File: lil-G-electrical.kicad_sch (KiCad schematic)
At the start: 39 parts, among them J1 GPIO, J2 XT-60, Q1 STD26P3LLH6, SW1 B3J-1000, SW2 PVA1EE, U1 TPS565208, U2 CAT24C256, U3 LTC2955-1, U4 MCP1415

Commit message: small update on schematic
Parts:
- renumbered C13 to C1, C3 to C10, C5 to C11, C6 to C12, C7 to C13, C11 to C2, C8 to C3, C10 to C4, C12 to C5, C9 to C6, C4 to C7, C1 to C8, C2 to C9, J2 to J1, J1 to J2, R6 to R1, R2 to R10, R3 to R11, R4 to R12, R8 to R2, R10 to R3, R12 to R4, R7 to R5, R9 to R6, R11 to R7, R5 to R8, R1 to R9, U3 to U1, U4 to U2, U1 to U3, U2 to U4
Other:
- moved on the sheet: C13, JP1, R11, R12, U4

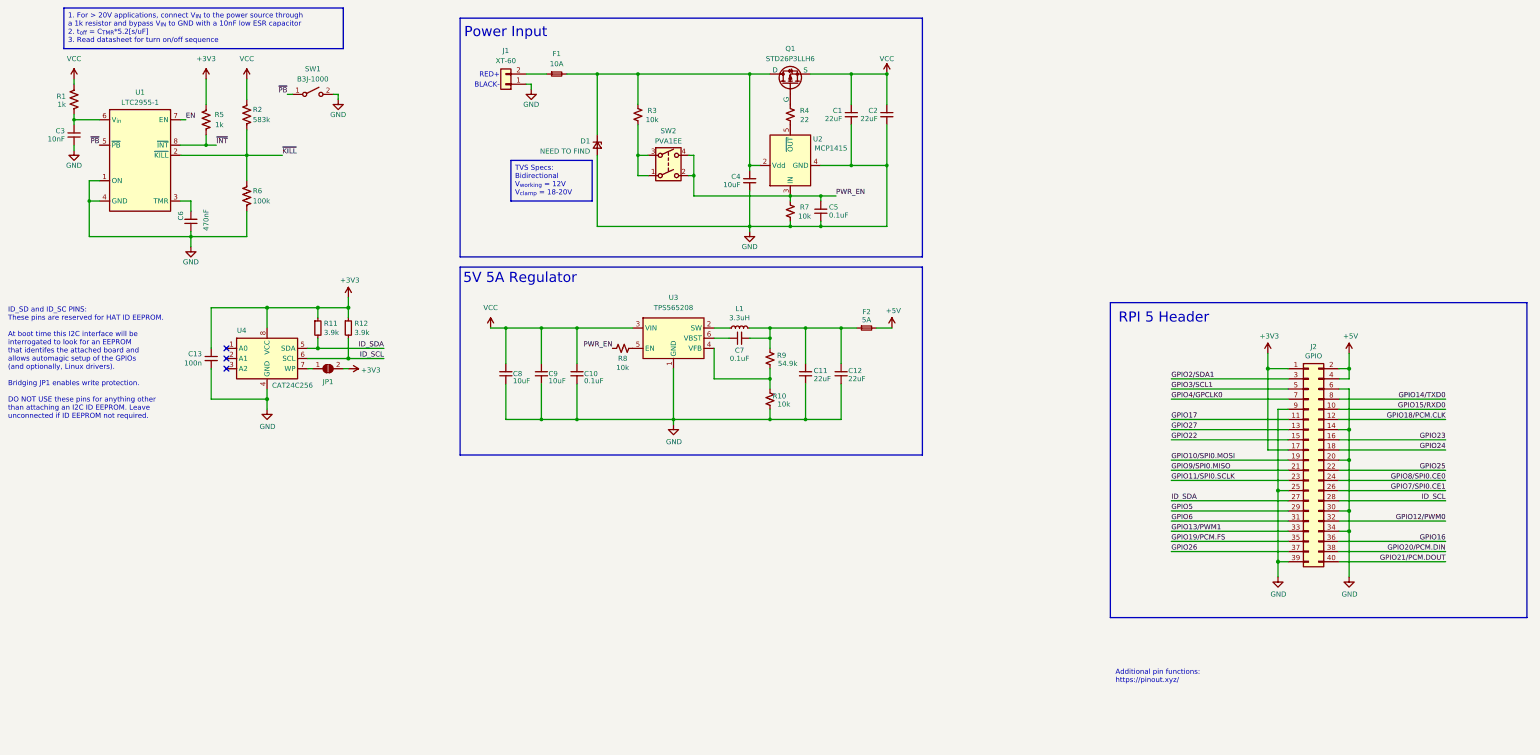
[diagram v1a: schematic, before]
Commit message: finished layout of dc drivers and power regulation
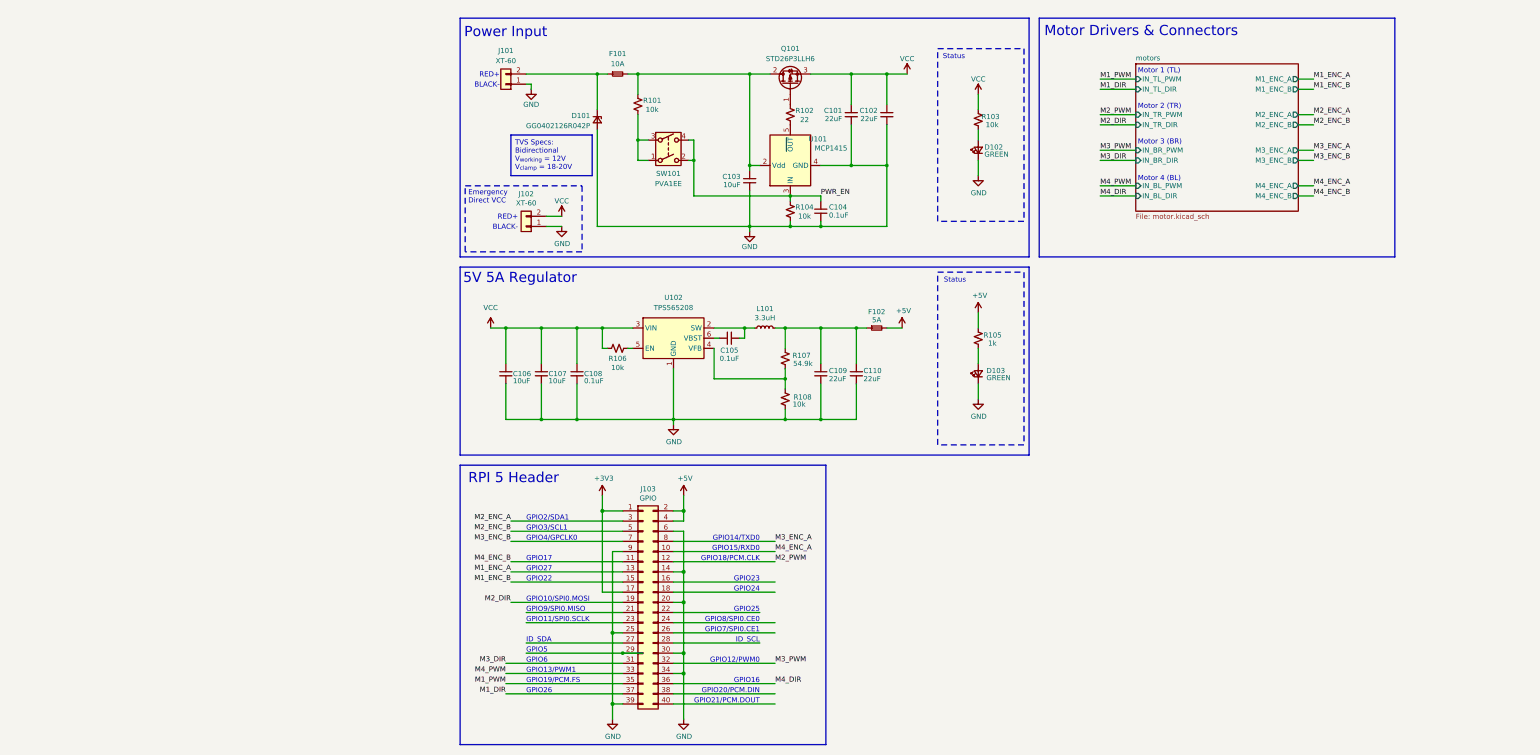
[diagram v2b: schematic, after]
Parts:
- removed C13: 100n, symbol Device:C_Small
- removed C3: 10nF, Capacitor_SMD:C_0603_1608Metric, symbol Device:C_Small
- removed C6: 470nF, Capacitor_SMD:C_1206_3216Metric, symbol Device:C_Small
- removed JP1: ID_WP, symbol Jumper:SolderJumper_2_Open
- removed Q1: STD26P3LLH6, Package_TO_SOT_SMD:TO-252-2, symbol Simulation_SPICE:PMOS
- removed R1, R5: 1k, Resistor_SMD:R_0603_1608Metric, symbol Device:R_US
- removed R11, R12: 3.9k, symbol Device:R_Small
- removed R2: 583k, Resistor_SMD:R_0603_1608Metric, symbol Device:R_US
- removed R6: 100k, Resistor_SMD:R_0603_1608Metric, symbol Device:R_US
- removed SW1: B3J-1000, RoboJackets-Switches:B3J-1000, symbol Switch:SW_SPST
- removed U1: LTC2955-1, RoboJackets-Power:SOT65P280X100-8N, symbol RoboJackets-Power:LTC2955-1
- removed U4: CAT24C256, symbol Memory_EEPROM:CAT24C256
- added D102, D103: GREEN, LED_SMD:LED_0603_1608Metric, symbol Device:LED_Small
- added J102: XT-60, Connector_AMASS:AMASS_XT60-M_1x02_P7.20mm_Vertical, symbol Connector_Generic:Conn_01x02
- added Q101: STD26P3LLH6, Package_TO_SOT_SMD:TO-252-2, symbol Device:Q_PMOS_GDS
- added R103: 10k, Resistor_SMD:R_0603_1608Metric, symbol Device:R_Small_US
- added R105: 1k, Resistor_SMD:R_0603_1608Metric, symbol Device:R_Small_US
- D101: renamed from D1; value NEED TO FIND -> GG0402126R042P; footprint Diode_SMD:D_0603_1608Metric -> Diode_SMD:D_0402_1005Metric
- F102: renamed from F2; footprint lilG_footprints:LittleFuse_Mini_100_SMD -> Fuse:Fuse_0603_1608Metric; MPN (none) -> F0603SB5000V032TM
- R101: renamed from R3; footprint (none) -> Resistor_SMD:R_0603_1608Metric
- R102: renamed from R4; footprint (none) -> Resistor_SMD:R_0603_1608Metric
- R104: renamed from R7; footprint (none) -> Resistor_SMD:R_0603_1608Metric
- R106: renamed from R8; footprint (none) -> Resistor_SMD:R_0603_1608Metric
- R107: renamed from R9; footprint (none) -> Resistor_SMD:R_0603_1608Metric
- R108: renamed from R10; footprint (none) -> Resistor_SMD:R_0603_1608Metric
- U102: renamed from U3; footprint Package_SO:Texas_R-PDSO-G8_EP2.95x4.9mm_Mask2.4x3.1mm -> Package_TO_SOT_SMD:SOT-23-6
- renumbered C1 to C101, C2 to C102, C4 to C103, C5 to C104, C7 to C105, C8 to C106, C9 to C107, C10 to C108, C11 to C109, C12 to C110, F1 to F101, J1 to J101, J2 to J103, L1 to L101, SW2 to SW101, U2 to U101
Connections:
- net +5V: now also R105.2
- net GND: now also D102.1 (K), D103.1 (K), J102.1 (Pin_1)
- net PWR_EN: no longer R106.2
- net VCC: now also R106.2, J102.2 (Pin_2), Q101.3 (S), R103.2
- net at C103.1, F101.2, R101.1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: now also Q101.2 (D); no longer D101.1 (K)
- net at F101.1, J101.2 (Pin_2): now also D101.1 (K)
- net at C109.1, C110.1, F102.1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: no longer C105.1
- net at L101.1, U102.2 (SW): now also C105.1
- net at R102.1: now also Q101.1 (G)
- net GPIO10/SPI0.MOSI renamed M2_DIR
- net GPIO11/SPI0.SCLK: no longer names the net of J103.23 (Pin_23)
- net GPIO12/PWM0 renamed M3_PWM
- net GPIO13/PWM1 renamed M4_PWM
- net GPIO14/TXD0 renamed M3_ENC_A
- net GPIO15/RXD0 renamed M4_ENC_A
- net GPIO16 renamed M4_DIR
- net GPIO17 renamed M4_ENC_B
- net GPIO18/PCM.CLK renamed M2_PWM
- net GPIO19/PCM.FS renamed M1_PWM
- net GPIO20/PCM.DIN: no longer names the net of J103.38 (Pin_38)
- net GPIO21/PCM.DOUT: no longer names the net of J103.40 (Pin_40)
- net GPIO22 renamed M1_ENC_B
- net GPIO23: no longer names the net of J103.16 (Pin_16)
- net GPIO24: no longer names the net of J103.18 (Pin_18)
- net GPIO25: no longer names the net of J103.22 (Pin_22)
- net GPIO26 renamed M1_DIR
- net GPIO27 renamed M1_ENC_A
- net GPIO2/SDA1 renamed M2_ENC_A
- net GPIO3/SCL1 renamed M2_ENC_B
- net GPIO4/GPCLK0 renamed M3_ENC_B
- net GPIO5: no longer names the net of J103.29 (Pin_29)
- net GPIO6 renamed M3_DIR
- net GPIO7/SPI0.CE1: no longer names the net of J103.26 (Pin_26)
- net GPIO8/SPI0.CE0: no longer names the net of J103.24 (Pin_24)
- net GPIO9/SPI0.MISO: no longer names the net of J103.21 (Pin_21)
- net ID_SCL: no longer names the net of J103.28 (Pin_28)
- net ID_SDA: no longer names the net of J103.27 (Pin_27)
- new net: D102.2 (A), R103.1
- new net: D103.2 (A), R105.1
- no-connect marks 3 -> 0
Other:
- added sheet motors (motor.kicad_sch)
- note added: "Emergency Direct VCC"
- note added: "GPIO10/SPI0.MOSI"
- note added: "GPIO11/SPI0.SCLK"
- note added: "GPIO12/PWM0"
- note added: "GPIO13/PWM1"
- note added: "GPIO14/TXD0"
- note added: "GPIO15/RXD0"
- note added: "GPIO16"
- note added: "GPIO17"
- note added: "GPIO18/PCM.CLK"
- note added: "GPIO19/PCM.FS"
- note added: "GPIO2/SDA1"
- note added: "GPIO20/PCM.DIN"
- note added: "GPIO21/PCM.DOUT"
- note added: "GPIO22"
- note added: "GPIO23"
- note added: "GPIO24"
- note added: "GPIO25"
- note added: "GPIO26"
- note added: "GPIO27"
- note added: "GPIO3/SCL1"
- note added: "GPIO4/GPCLK0"
- note added: "GPIO5"
- note added: "GPIO6"
- note added: "GPIO7/SPI0.CE1"
- note added: "GPIO8/SPI0.CE0"
- note added: "GPIO9/SPI0.MISO"
- note added: "ID_SCL"
- note added: "ID_SDA"
- note added: "Motor 1 (TL)"
- note added: "Motor 2 (TR)"
- note added: "Motor 3 (BR)"
- note added: "Motor 4 (BL)"
- note added: "Motor Drivers & Connectors"
- note added: "Status"
- note removed: "Additional pin functions: https://pinout.xyz/"
- note removed: "ID_SD and ID_SC PINS: These pins are reserved for HAT ID EEPROM. At boot time this I2C interface will be interrogated to look for an EEPROM that identifes the attached board and allows automagic setup of the GPIOs (and optionally, Linux drivers). Bridging JP1 enables write protection. DO NOT USE these pins for anything other than attaching an I2C ID EEPROM. Leave unconnected if ID EEPROM not requ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"
- moved on the sheet: C105, C109, C110, D101, F101, F102, J103, L101, R101, R106, R107, R108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

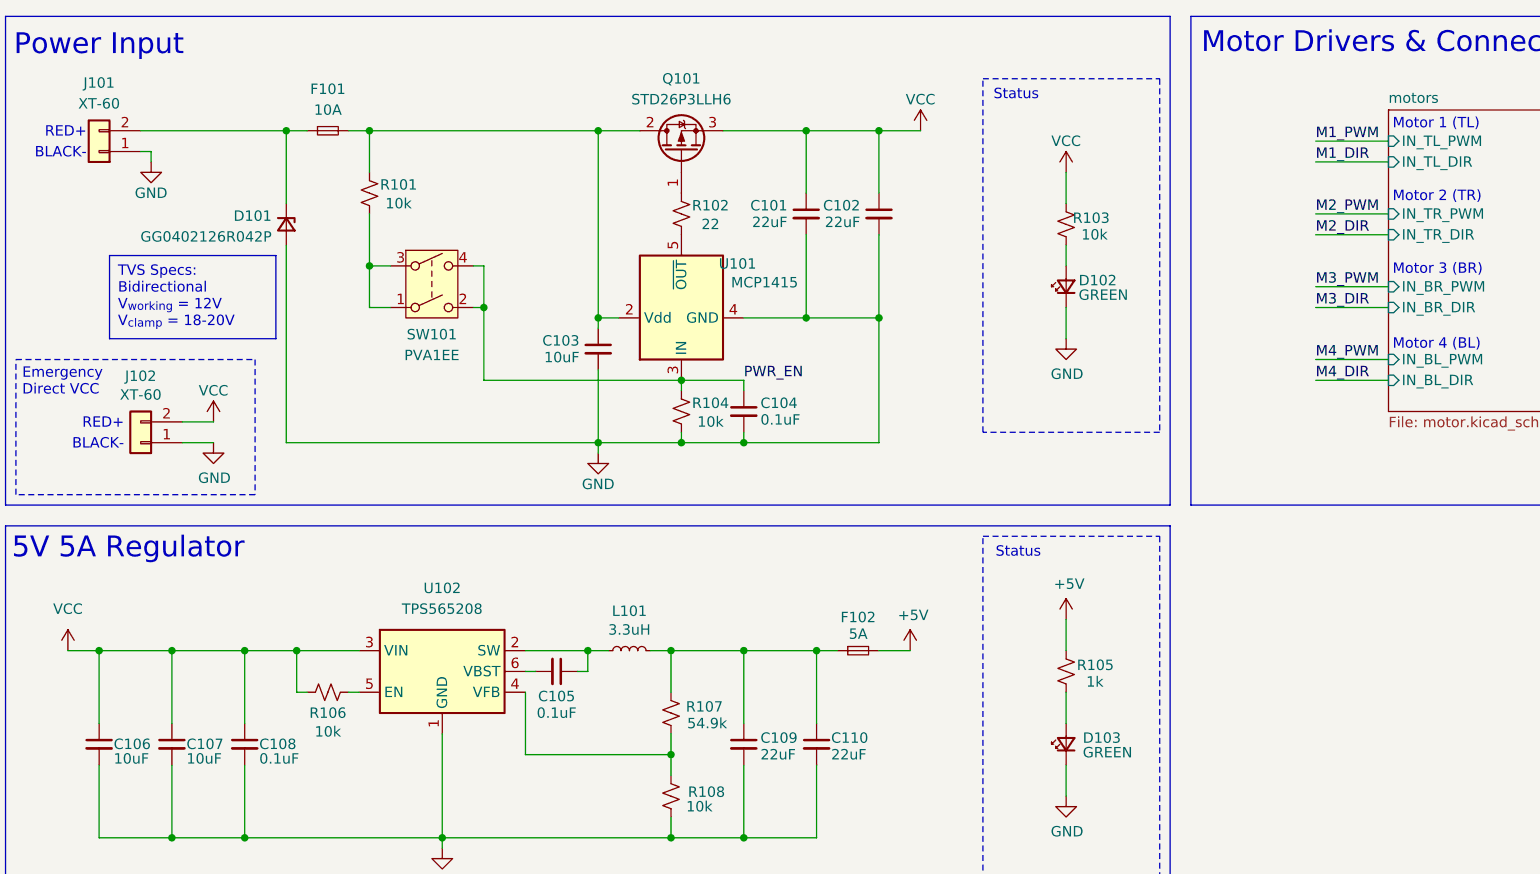
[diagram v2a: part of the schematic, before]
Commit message: changed dimension of current sense resistor
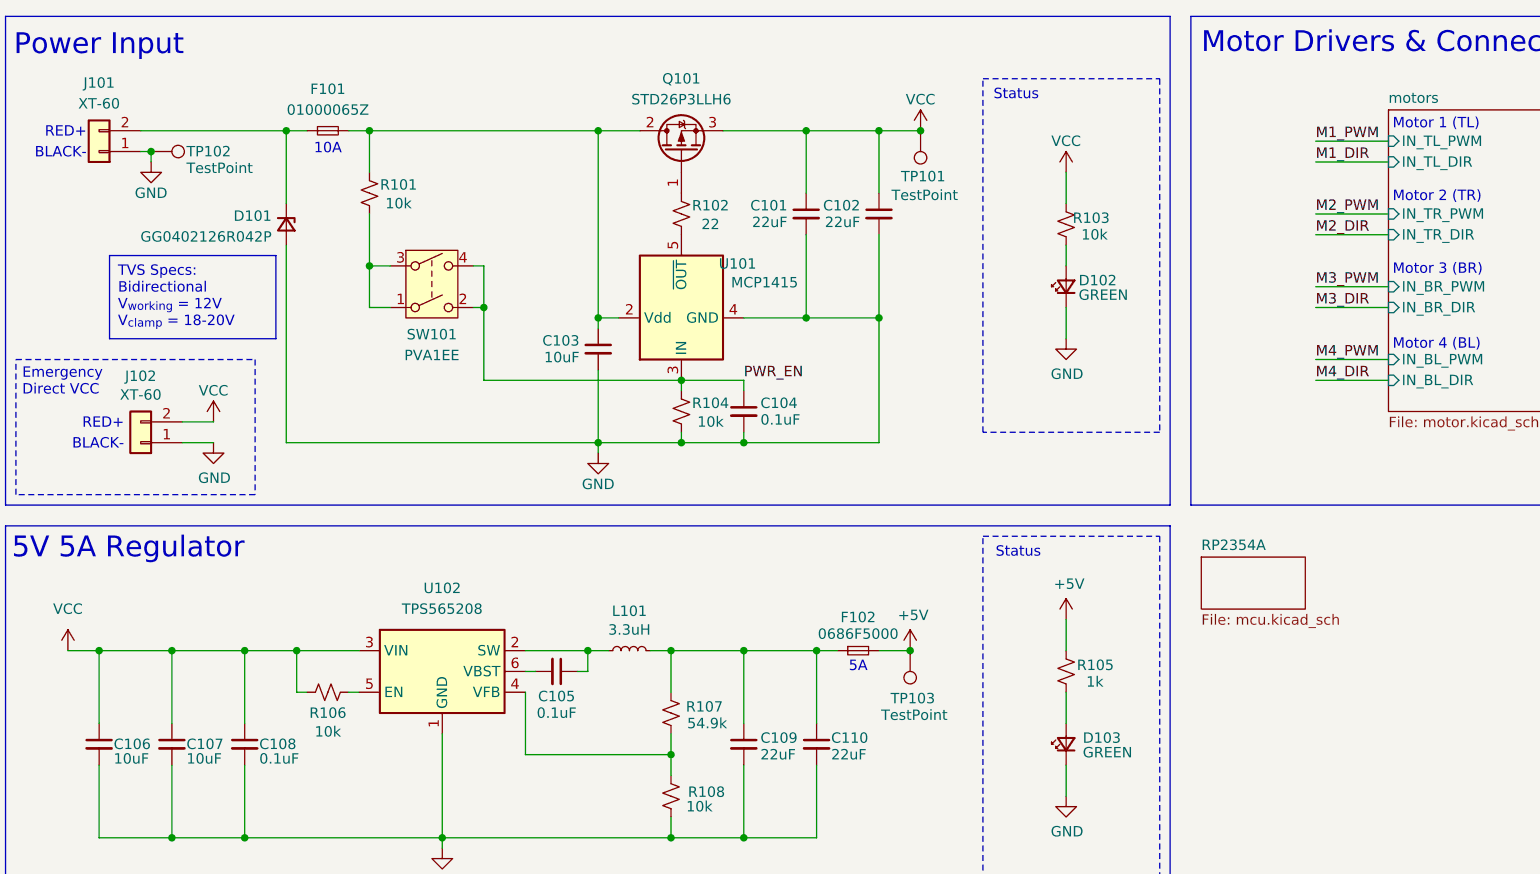
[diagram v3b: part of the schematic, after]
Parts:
- added TP101, TP102, TP103: TestPoint, TestPoint:TestPoint_Keystone_5000-5004_Miniature, symbol Connector:TestPoint
- C101, C102, C109, C110: footprint Capacitor_SMD:C_0603_1608Metric -> Capacitor_SMD:C_0805_2012Metric
- F101: value 10A -> 01000065Z
- F102: value 5A -> 0686F5000
- J101, J102, J103, SW101: now left out of the parts list
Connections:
- net +5V: now also TP103.1
- net GND: now also TP102.1
- net VCC: now also TP101.1
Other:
- added sheet RP2354A (mcu.kicad_sch)
- note added: "10A"
- note added: "5A"
